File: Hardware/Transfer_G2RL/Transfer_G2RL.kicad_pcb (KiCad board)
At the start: 2 copper layers, 88.3 x 71.4 mm, 20 parts, among them J1 Screw_Terminal_01x02, J5 SO-239, J6 SO-239, J7 SO-239, J8 SO-239, K2 G2RL-1-E, K3 G2RL-1-E

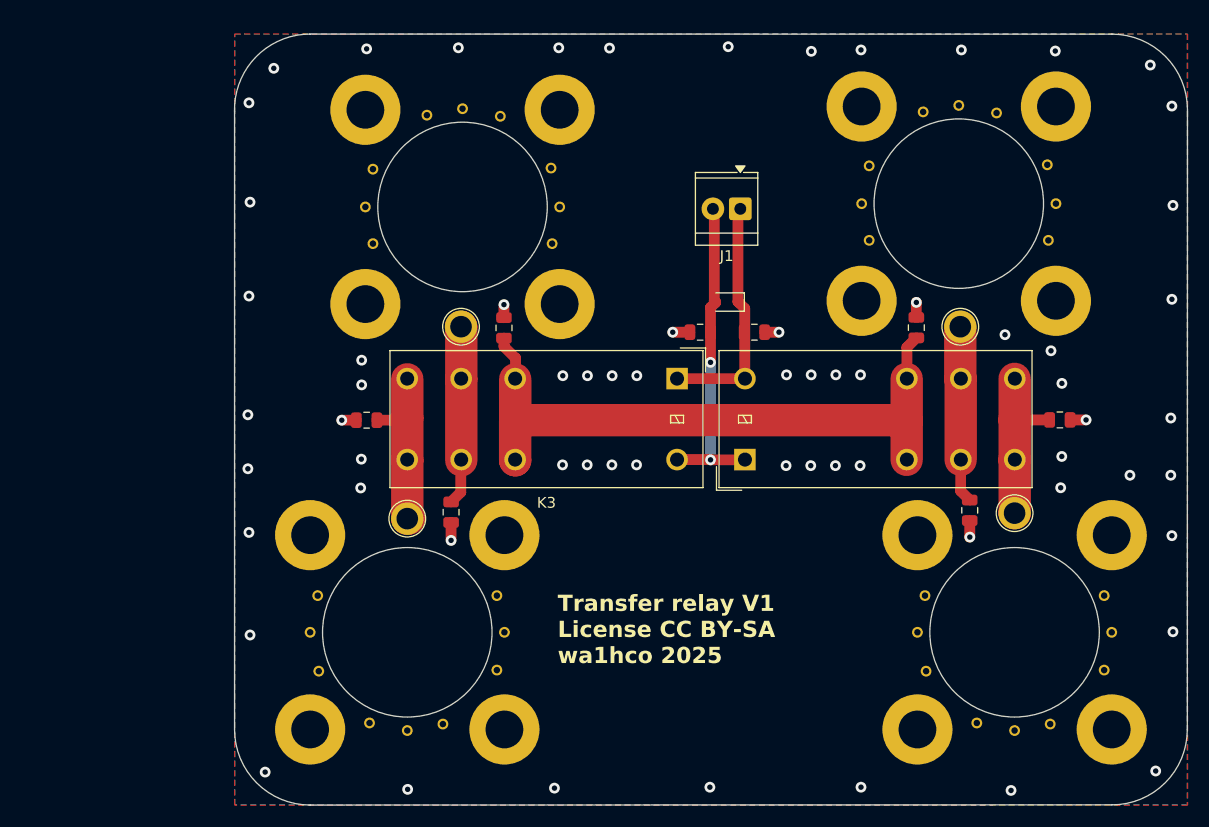
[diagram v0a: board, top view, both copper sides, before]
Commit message: Added drilling dimensions for Transfer Relay enclosure Added ethernet cable color codes to schematic, validated that part Validated KEY/ input to interlock works Validated KEY/ input inhibits lower priority radio and lites Inhibit LED Added rippling LED's to setup() code
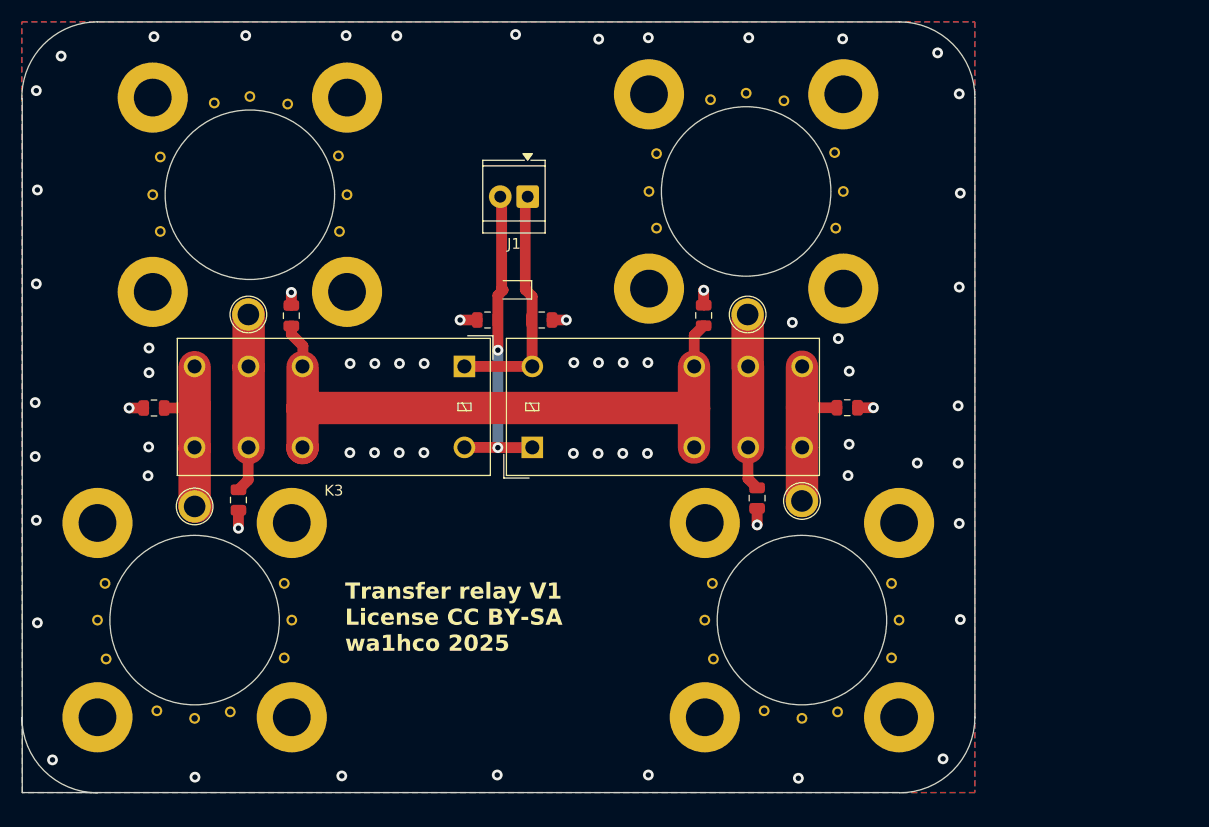
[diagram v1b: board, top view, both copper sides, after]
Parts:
- moved C1 19.7 mm to (141.5, 107.3)
- moved C6 19.7 mm to (149.8, 98.9)
- moved H4 19.7 mm to (140.6, 90.3)
- moved C3 19.7 mm to (98.3, 90.4)
- moved C4 19.7 mm to (85.6, 99.0)
- moved C5 19.7 mm to (93.4, 107.5)
- moved D1 19.7 mm to (119.0, 88.0)
- moved H2 19.7 mm to (94.3, 90.3)
- moved H3 19.7 mm to (89.4, 108.1)
- moved J7 19.7 mm to (89.4, 118.6)
- moved J8 19.7 mm to (94.5, 79.2)
- moved K3 19.7 mm to (94.5, 98.9)
- moved C14 19.7 mm to (116.5, 90.8)
- moved C2 19.7 mm to (136.5, 90.4)
- moved C8 19.7 mm to (121.5, 90.8)
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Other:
- outline, holes or cut-outs redrawn
